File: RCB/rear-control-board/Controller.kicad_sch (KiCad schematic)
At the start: 27 parts, among them J6 Conn_01x05, U1 STM32F413CGUx, U2 LD1117S33TR_SOT223, U4 MCP2551-I-SN, Y1 Crystal

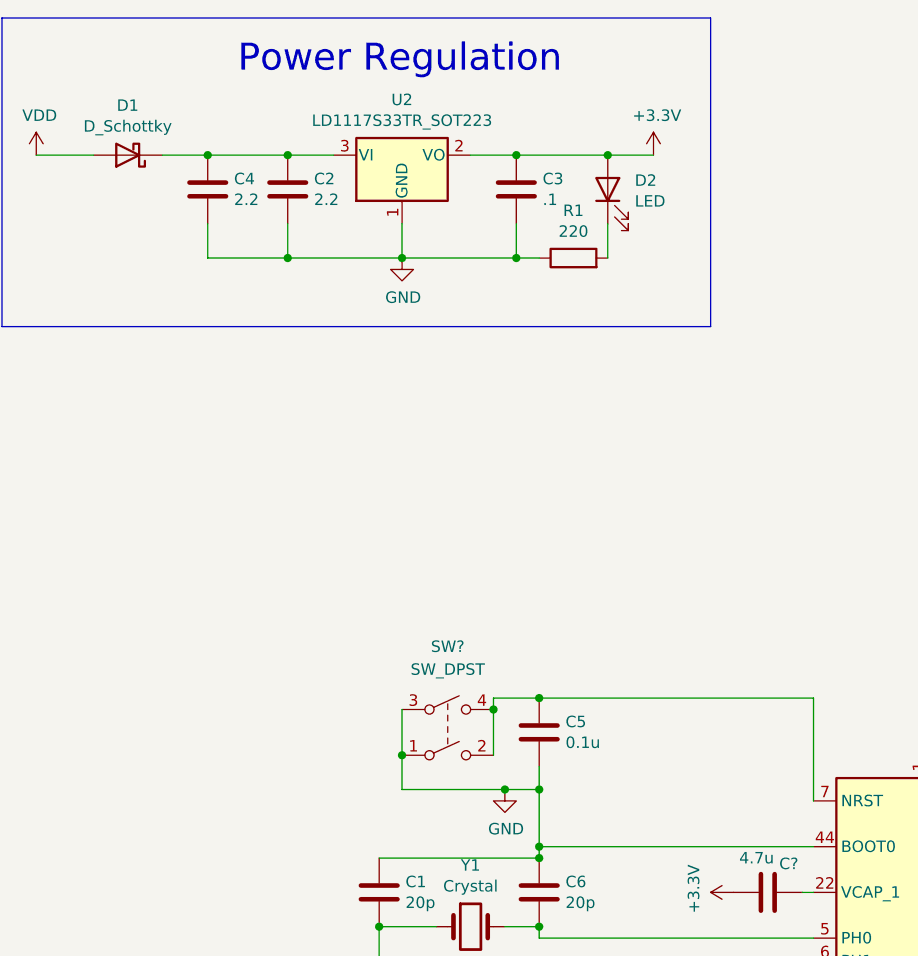
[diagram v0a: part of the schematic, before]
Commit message: power filtering and notes
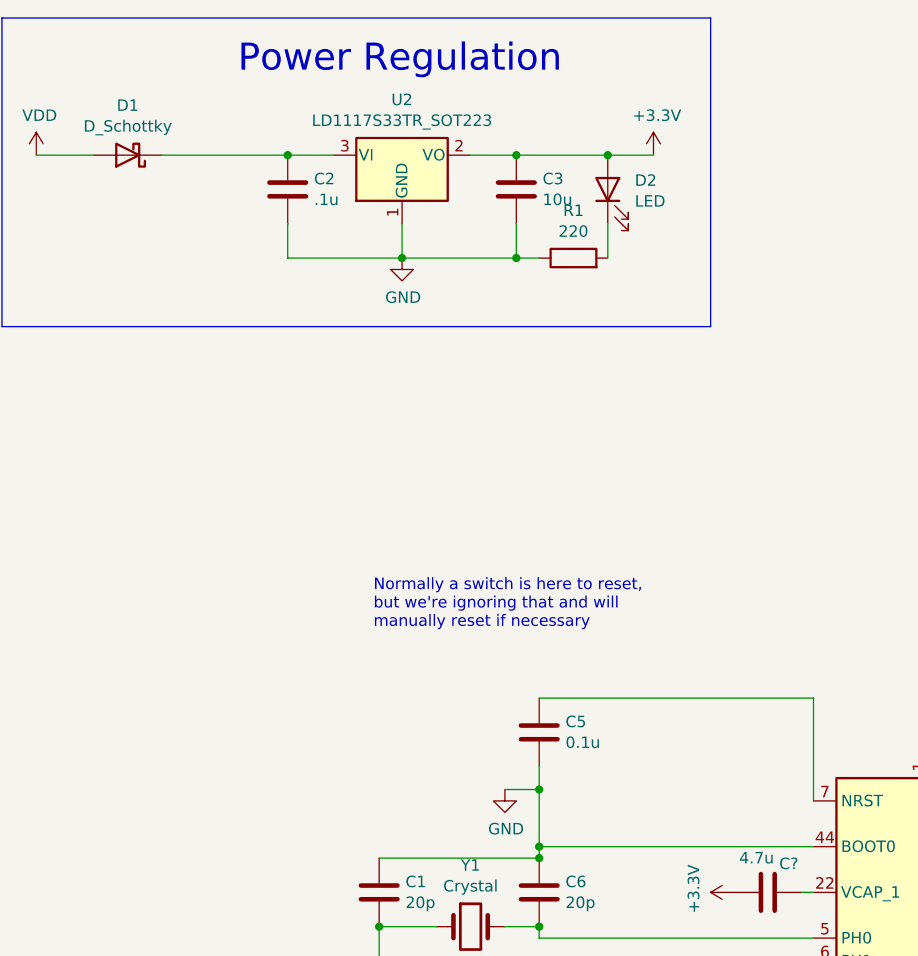
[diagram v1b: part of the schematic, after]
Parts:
- removed C4: 2.2, Capacitor_SMD:C_0603_1608Metric_Pad1.08x0.95mm_HandSolder, symbol Device:C
- removed SW?: SW_DPST, symbol Switch:SW_DPST
- C2: value 2.2 -> .1u
- C3: value .1 -> 10u
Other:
- note added: "Normally a switch is here to reset, but we're ignoring that and will manually reset if necessary"
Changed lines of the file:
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@@
   (junction (at 77.47 107.315) (diameter 0) (color 0 0 0 0)
   )
-  (junction (at 40.64 29.21) (diameter 0) (color 0 0 0 0)
-  )
   (junction (at 166.37 95.885) (diameter 0) (color 0 0 0 0)
   )
@@
   (junction (at 125.73 177.165) (diameter 0) (color 0 0 0 0)
   )
-  (junction (at 72.39 90.805) (diameter 0) (color 0 0 0 0)
-  )
-  (junction (at 77.47 89.535) (diameter 0) (color 0 0 0 0)
-  )
   (junction (at 269.24 152.4) (diameter 0) (color 0 0 0 0)
   )
-  (junction (at 73.66 99.695) (diameter 0) (color 0 0 0 0)
-  )
   (junction (at 74.93 29.21) (diameter 0) (color 0 0 0 0)
   )
@@
   (junction (at 123.19 177.165) (diameter 0) (color 0 0 0 0)
   )
-  (junction (at 62.23 95.885) (diameter 0) (color 0 0 0 0)
-  )
   (junction (at 269.24 128.27) (diameter 0) (color 0 0 0 0)
   )
@@
   (junction (at 77.47 99.695) (diameter 0) (color 0 0 0 0)
   )
-  (junction (at 49.53 40.64) (diameter 0) (color 0 0 0 0)
-  )
   (wire (pts (xy 234.95 153.67) (xy 251.46 153.67))
     (stroke (width 0) (type default) (color 0 0 0 0))
@@
     (stroke (width 0) (type default) (color 0 0 0 0))
   )
-  (wire (pts (xy 72.39 89.535) (xy 77.47 89.535))
-    (stroke (width 0) (type default) (color 0 0 0 0))
-  )
   (wire (pts (xy 274.955 125.73) (xy 275.59 125.73))
     (stroke (width 0) (type default) (color 0 0 0 0))
@@
     (stroke (width 0) (type default) (color 0 0 0 0))
   )
-  (wire (pts (xy 62.23 95.885) (xy 62.23 99.695))
-    (stroke (width 0) (type default) (color 0 0 0 0))
-  )
   (wire (pts (xy 144.78 141.605) (xy 140.97 141.605))
     (stroke (width 0) (type default) (color 0 0 0 0))
@@
     (stroke (width 0) (type default) (color 0 0 0 0))
   )
-  (wire (pts (xy 72.39 90.805) (xy 72.39 95.885))
-    (stroke (width 0) (type default) (color 0 0 0 0))
-  )
   (wire (pts (xy 166.37 81.915) (xy 171.45 81.915))
     (stroke (width 0) (type default) (color 0 0 0 0))
@@
     (stroke (width 0) (type default) (color 0 0 0 0))
   )
-  (wire (pts (xy 35.56 29.21) (xy 40.64 29.21))
-    (stroke (width 0) (type default) (color 0 0 0 0))
-  )
   (wire (pts (xy 120.65 177.165) (xy 120.65 174.625))
     (stroke (width 0) (type default) (color 0 0 0 0))
@@
     (stroke (width 0) (type default) (color 0 0 0 0))
   )
-  (wire (pts (xy 62.23 90.805) (xy 62.23 95.885))
-    (stroke (width 0) (type default) (color 0 0 0 0))
-  )
   (wire (pts (xy 140.97 136.525) (xy 144.78 136.525))
     (stroke (width 0) (type default) (color 0 0 0 0))
@@
     (stroke (width 0) (type default) (color 0 0 0 0))
   )
-  (wire (pts (xy 40.64 29.21) (xy 49.53 29.21))
+  (wire (pts (xy 35.56 29.21) (xy 49.53 29.21))
     (stroke (width 0) (type default) (color 0 0 0 0))
   )
@@
     (stroke (width 0) (type default) (color 0 0 0 0))
   )
-  (wire (pts (xy 40.64 40.64) (xy 49.53 40.64))
-    (stroke (width 0) (type default) (color 0 0 0 0))
-  )
   (wire (pts (xy 150.495 159.385) (xy 140.97 159.385))
     (stroke (width 0) (type default) (color 0 0 0 0))
@@
     (stroke (width 0) (type default) (color 0 0 0 0))
   )
-  (wire (pts (xy 62.23 99.695) (xy 73.66 99.695))
-    (stroke (width 0) (type default) (color 0 0 0 0))
-  )
   (polyline (pts (xy 278.13 161.29) (xy 278.13 109.22))
     (stroke (width 0) (type default) (color 0 0 0 0))
@@
     (stroke (width 0) (type default) (color 0 0 0 0))
   )
-  (wire (pts (xy 40.64 36.83) (xy 40.64 40.64))
-    (stroke (width 0) (type default) (color 0 0 0 0))
-  )
   (polyline (pts (xy 96.52 48.26) (xy 17.78 48.26))
     (stroke (width 0) (type default) (color 0 0 0 0))
@@
   )
   (wire (pts (xy 140.97 149.225) (xy 154.305 149.225))
-    (stroke (width 0) (type default) (color 0 0 0 0))
-  )
-  (wire (pts (xy 72.39 89.535) (xy 72.39 90.805))
     (stroke (width 0) (type default) (color 0 0 0 0))
   )
@@
   (text "CAN Transceiver" (at 242.57 114.3 0)
     (effects (font (size 2.0066 2.0066)) (justify left bottom))
+  )
+  (text "Normally a switch is here to reset,\nbut we're ignoring that and will \nmanually reset if necessary"
+    (at 59.055 81.915 0)
+    (effects (font (size 1.27 1.27)) (justify left bottom))
   )
   (text "IMD is low when clear, pull high\nBMS is high when clear, pull low"
@@
       (effects (font (size 1.27 1.27)) (justify left))
     )
-    (property "Value" "2.2" (id 1) (at 52.451 34.163 0)
+    (property "Value" ".1u" (id 1) (at 52.451 34.163 0)
       (effects (font (size 1.27 1.27)) (justify left))
     )
@@
       (effects (font (size 1.27 1.27)) (justify left))
     )
-    (property "Value" ".1" (id 1) (at 77.851 34.163 0)
+    (property "Value" "10u" (id 1) (at 77.851 34.163 0)
       (effects (font (size 1.27 1.27)) (justify left))
     )
@@
     (pin "2")
   )
-  (symbol (lib_id "Switch:SW_DPST") (at 67.31 93.345 0) (unit 1)
-    (in_bom yes) (on_board yes) (fields_autoplaced)
-    (property "Reference" "SW?" (id 0) (at 67.31 83.82 0))
-    (property "Value" "SW_DPST" (id 1) (at 67.31 86.36 0))
-    (property "Footprint" "" (id 2) (at 67.31 93.345 0)
-      (effects (font (size 1.27 1.27)) hide)
-    )
-    (property "Datasheet" "~" (id 3) (at 67.31 93.345 0)
-      (effects (font (size 1.27 1.27)) hide)
-    )
-    (pin "1")
-    (pin "2")
-    (pin "3")
-    (pin "4")
-  )
   (symbol (lib_id "power:+3.3V") (at 99.06 111.125 90) (unit 1)
     (in_bom yes) (on_board yes)
@@
     (pin "1")
   )
-  (symbol (lib_id "Device:C") (at 40.64 33.02 0) (unit 1)
-    (in_bom yes) (on_board yes)
-    (property "Reference" "C4" (id 0) (at 43.561 31.8516 0)
-      (effects (font (size 1.27 1.27)) (justify left))
-    )
-    (property "Value" "2.2" (id 1) (at 43.561 34.163 0)
-      (effects (font (size 1.27 1.27)) (justify left))
-    )
-    (property "Footprint" "Capacitor_SMD:C_0603_1608Metric_Pad1.08x0.95mm_HandSolder" (id 2) (at 41.6052 36.83 0)
-      (effects (font (size 1.27 1.27)) hide)
-    )
-    (property "Datasheet" "~" (id 3) (at 40.64 33.02 0)
-      (effects (font (size 1.27 1.27)) hide)
-    )
-    (pin "1")
-    (pin "2")
-  )
 )

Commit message: updating filtering cap layout
Kay suggested layout changes. Moved caps around
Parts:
- gave numbers to parts that had none: 1
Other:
- note added: "Power Caps Place as close as possible to the VDD pins"
- note removed: "Power Caps"
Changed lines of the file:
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@@
     (effects (font (size 2.9972 2.9972)) (justify left bottom))
   )
-  (text "Power Caps" (at 162.56 73.025 0)
+  (text "Power Caps\nPlace as close as possible to the VDD pins"
+    (at 154.305 73.66 0)
     (effects (font (size 1.27 1.27)) (justify left bottom))
   )
@@
   (symbol (lib_id "power:+3.3V") (at 99.06 111.125 90) (unit 1)
     (in_bom yes) (on_board yes)
-    (property "Reference" "#PWR?" (id 0) (at 102.87 111.125 0)
+    (property "Reference" "#PWR0142" (id 0) (at 102.87 111.125 0)
       (effects (font (size 1.27 1.27)) hide)
     )
@@
   (symbol (lib_id "Device:C") (at 102.87 111.125 270) (unit 1)
     (in_bom yes) (on_board yes)
-    (property "Reference" "C?" (id 0) (at 104.14 107.95 90)
-      (effects (font (size 1.27 1.27)) (justify left))
-    )
+    (property "Reference" "C4" (id 0) (at 104.14 107.95 90)
+      (effects (font (size 1.27 1.27)) (justify left))
+    )

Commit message: Major Review and Part Update
updating footprints, component values, layouts
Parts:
- removed C1, C6: 20p, Capacitor_SMD:C_0603_1608Metric_Pad1.08x0.95mm_HandSolder, symbol Device:C
- removed C8: 0.1u, Capacitor_SMD:C_0603_1608Metric_Pad1.08x0.95mm_HandSolder, symbol Device:C
- removed Y1: Crystal, Crystal:Crystal_HC49-U_Vertical, symbol Device:Crystal
- added Y1: CSTNE8M00, AERO_Footprints:Resonator_SMD_muRata_CSTxExxV-3Pin_3.0x1.1mm_HandSoldering, symbol Device:Resonator
- D1: value D_Schottky -> BAT54GW
- R1: value 220 -> 330
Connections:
- net GND: now also U1.8 (VSSA), Y1.2
- net at U1.5 (PH0): now also Y1.1
- net at U1.6 (PH1): now also Y1.3
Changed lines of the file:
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@@
 (kicad_sch (version 20211123) (generator eeschema)
   (paper "A4")
-  (junction (at 77.47 107.315) (diameter 0) (color 0 0 0 0)
+  (junction (at 128.27 177.165) (diameter 0) (color 0 0 0 0)
   )
   (junction (at 166.37 95.885) (diameter 0) (color 0 0 0 0)
@@
   (junction (at 80.01 136.525) (diameter 0) (color 0 0 0 0)
   )
-  (junction (at 140.97 84.455) (diameter 0) (color 0 0 0 0)
-  )
-  (junction (at 77.47 114.935) (diameter 0) (color 0 0 0 0)
-  )
   (junction (at 125.73 90.805) (diameter 0) (color 0 0 0 0)
   )
   (junction (at 80.01 133.985) (diameter 0) (color 0 0 0 0)
   )
-  (junction (at 59.69 114.935) (diameter 0) (color 0 0 0 0)
-  )
   (junction (at 49.53 29.21) (diameter 0) (color 0 0 0 0)
   )
@@
   (junction (at 166.37 81.915) (diameter 0) (color 0 0 0 0)
   )
-  (junction (at 143.51 92.075) (diameter 0) (color 0 0 0 0)
-  )
   (junction (at 77.47 106.045) (diameter 0) (color 0 0 0 0)
   )
@@
     (stroke (width 0) (type default) (color 0 0 0 0))
   )
-  (wire (pts (xy 140.97 84.455) (xy 146.05 84.455))
-    (stroke (width 0) (type default) (color 0 0 0 0))
-  )
   (wire (pts (xy 274.955 125.73) (xy 275.59 125.73))
     (stroke (width 0) (type default) (color 0 0 0 0))
@@
     (stroke (width 0) (type default) (color 0 0 0 0))
   )
-  (wire (pts (xy 77.47 114.935) (xy 73.66 114.935))
-    (stroke (width 0) (type default) (color 0 0 0 0))
-  )
   (wire (pts (xy 85.09 40.64) (xy 85.09 36.83))
     (stroke (width 0) (type default) (color 0 0 0 0))
@@
     (stroke (width 0) (type default) (color 0 0 0 0))
   )
-  (wire (pts (xy 59.69 114.935) (xy 66.04 114.935))
-    (stroke (width 0) (type default) (color 0 0 0 0))
-  )
-  (wire (pts (xy 143.51 92.075) (xy 146.05 92.075))
-    (stroke (width 0) (type default) (color 0 0 0 0))
-  )
   (wire (pts (xy 171.45 81.915) (xy 171.45 84.455))
     (stroke (width 0) (type default) (color 0 0 0 0))
@@
     (stroke (width 0) (type default) (color 0 0 0 0))
   )
-  (wire (pts (xy 59.69 118.745) (xy 107.95 118.745))
-    (stroke (width 0) (type default) (color 0 0 0 0))
-  )
   (wire (pts (xy 107.95 89.535) (xy 107.95 100.965))
     (stroke (width 0) (type default) (color 0 0 0 0))
@@
     (stroke (width 0) (type default) (color 0 0 0 0))
   )
+  (wire (pts (xy 73.66 107.315) (xy 77.47 107.315))
+    (stroke (width 0) (type default) (color 0 0 0 0))
+  )
   (polyline (pts (xy 128.905 18.415) (xy 128.905 54.61))
     (stroke (width 0) (type default) (color 0 0 0 0))
@@
     (stroke (width 0) (type default) (color 0 0 0 0))
   )
+  (wire (pts (xy 128.27 177.165) (xy 130.81 177.165))
+    (stroke (width 0) (type default) (color 0 0 0 0))
+  )
   (polyline (pts (xy 17.78 13.97) (xy 96.52 13.97))
     (stroke (width 0) (type default) (color 0 0 0 0))
@@
     (stroke (width 0) (type default) (color 0 0 0 0))
   )
+  (wire (pts (xy 73.66 109.855) (xy 73.66 107.315))
+    (stroke (width 0) (type default) (color 0 0 0 0))
+  )
   (wire (pts (xy 62.23 40.64) (xy 74.93 40.64))
     (stroke (width 0) (type default) (color 0 0 0 0))
@@
     (stroke (width 0) (type default) (color 0 0 0 0))
   )
+  (wire (pts (xy 69.85 114.935) (xy 69.85 118.745))
+    (stroke (width 0) (type default) (color 0 0 0 0))
+  )
   (wire (pts (xy 144.78 144.145) (xy 140.97 144.145))
     (stroke (width 0) (type default) (color 0 0 0 0))
@@
     (stroke (width 0) (type default) (color 0 0 0 0))
   )
+  (wire (pts (xy 130.81 177.165) (xy 130.81 174.625))
+    (stroke (width 0) (type default) (color 0 0 0 0))
+  )
   (wire (pts (xy 80.01 133.985) (xy 107.95 133.985))
     (stroke (width 0) (type default) (color 0 0 0 0))
@@
     (stroke (width 0) (type default) (color 0 0 0 0))
   )
-  (wire (pts (xy 59.69 114.935) (xy 59.69 118.745))
-    (stroke (width 0) (type default) (color 0 0 0 0))
-  )
   (wire (pts (xy 150.495 159.385) (xy 140.97 159.385))
     (stroke (width 0) (type default) (color 0 0 0 0))
@@
     (stroke (width 0) (type default) (color 0 0 0 0))
   )
+  (wire (pts (xy 69.85 118.745) (xy 107.95 118.745))
+    (stroke (width 0) (type default) (color 0 0 0 0))
+  )
   (polyline (pts (xy 278.13 161.29) (xy 278.13 109.22))
     (stroke (width 0) (type default) (color 0 0 0 0))
   )
   (wire (pts (xy 140.97 139.065) (xy 144.78 139.065))
-    (stroke (width 0) (type default) (color 0 0 0 0))
-  )
-  (wire (pts (xy 77.47 107.315) (xy 59.69 107.315))
     (stroke (width 0) (type default) (color 0 0 0 0))
   )
@@
     (in_bom yes) (on_board yes)
     (property "Reference" "D1" (id 0) (at 31.75 23.6982 0))
-    (property "Value" "D_Schottky" (id 1) (at 31.75 26.0096 0))
+    (property "Value" "BAT54GW" (id 1) (at 31.75 26.0096 0))
     (property "Footprint" "Diode_SMD:D_SMB" (id 2) (at 31.75 29.21 0)
       (effects (font (size 1.27 1.27)) hide)
@@
   (symbol (lib_id "Device:R") (at 81.28 40.64 90) (unit 1)
     (in_bom yes) (on_board yes)
-    (property "Reference" "R1" (id 0) (at 81.28 35.3822 90))
-    (property "Value" "220" (id 1) (at 81.28 37.6936 90))
+    (property "Reference" "R1" (id 0) (at 81.28 38.1 90))
+    (property "Value" "330" (id 1) (at 81.28 40.64 90))
     (property "Footprint" "Resistor_SMD:R_0603_1608Metric_Pad0.98x0.95mm_HandSolder" (id 2) (at 81.28 42.418 90)
       (effects (font (size 1.27 1.27)) hide)
@@
     )
     (pin "1")
-  )
-  (symbol (lib_id "Device:Crystal") (at 69.85 114.935 0) (unit 1)
-    (in_bom yes) (on_board yes)
-    (property "Reference" "Y1" (id 0) (at 69.85 108.1278 0))
-    (property "Value" "Crystal" (id 1) (at 69.85 110.4392 0))
-    (property "Footprint" "Crystal:Crystal_HC49-U_Vertical" (id 2) (at 69.85 114.935 0)
-      (effects (font (size 1.27 1.27)) hide)
-    )
-    (property "Datasheet" "~" (id 3) (at 69.85 114.935 0)
-      (effects (font (size 1.27 1.27)) hide)
-    )
-    (pin "1")
-    (pin "2")
-  )
-  (symbol (lib_id "Device:C") (at 59.69 111.125 0) (unit 1)
-    (in_bom yes) (on_board yes)
-    (property "Reference" "C1" (id 0) (at 62.611 109.9566 0)
-      (effects (font (size 1.27 1.27)) (justify left))
-    )
-    (property "Value" "20p" (id 1) (at 62.611 112.268 0)
-      (effects (font (size 1.27 1.27)) (justify left))
-    )
-    (property "Footprint" "Capacitor_SMD:C_0603_1608Metric_Pad1.08x0.95mm_HandSolder" (id 2) (at 60.6552 114.935 0)
-      (effects (font (size 1.27 1.27)) hide)
-    )
-    (property "Datasheet" "~" (id 3) (at 59.69 111.125 0)
-      (effects (font (size 1.27 1.27)) hide)
-    )
-    (pin "1")
-    (pin "2")
-  )
-  (symbol (lib_id "Device:C") (at 77.47 111.125 0) (unit 1)
-    (in_bom yes) (on_board yes)
-    (property "Reference" "C6" (id 0) (at 80.391 109.9566 0)
-      (effects (font (size 1.27 1.27)) (justify left))
-    )
-    (property "Value" "20p" (id 1) (at 80.391 112.268 0)
-      (effects (font (size 1.27 1.27)) (justify left))
-    )
-    (property "Footprint" "Capacitor_SMD:C_0603_1608Metric_Pad1.08x0.95mm_HandSolder" (id 2) (at 78.4352 114.935 0)
-      (effects (font (size 1.27 1.27)) hide)
-    )
-    (property "Datasheet" "~" (id 3) (at 77.47 111.125 0)
-      (effects (font (size 1.27 1.27)) hide)
-    )
-    (pin "1")
-    (pin "2")
   )
   (symbol (lib_id "power:+3.3V") (at 166.37 79.375 0) (unit 1)
@@
     (pin "1")
   )
-  (symbol (lib_id "Device:C") (at 146.05 88.265 180) (unit 1)
-    (in_bom yes) (on_board yes)
-    (property "Reference" "C8" (id 0) (at 151.13 89.535 0)
-      (effects (font (size 1.27 1.27)) (justify left))
-    )
-    (property "Value" "0.1u" (id 1) (at 152.4 86.995 0)
-      (effects (font (size 1.27 1.27)) (justify left))
-    )
-    (property "Footprint" "Capacitor_SMD:C_0603_1608Metric_Pad1.08x0.95mm_HandSolder" (id 2) (at 145.0848 84.455 0)
-      (effects (font (size 1.27 1.27)) hide)
-    )
-    (property "Datasheet" "~" (id 3) (at 146.05 88.265 0)
-      (effects (font (size 1.27 1.27)) hide)
-    )
-    (pin "1")
-    (pin "2")
-  )
   (symbol (lib_id "Device:C") (at 140.97 88.265 180) (unit 1)
     (in_bom yes) (on_board yes)
@@
     (pin "1")
   )
+  (symbol (lib_id "Device:Resonator") (at 73.66 114.935 180) (unit 1)
+    (in_bom yes) (on_board yes)
+    (property "Reference" "Y1" (id 0) (at 64.135 113.03 0))
+    (property "Value" "CSTNE8M00" (id 1) (at 64.77 109.22 0))
+    (property "Footprint" "AERO_Footprints:Resonator_SMD_muRata_CSTxExxV-3Pin_3.0x1.1mm_HandSoldering" (id 2) (at 74.295 114.935 0)
+      (effects (font (size 1.27 1.27)) hide)
+    )
+    (property "Datasheet" "~" (id 3) (at 74.295 114.935 0)
+      (effects (font (size 1.27 1.27)) hide)
+    )
+    (pin "1")
+    (pin "2")
+    (pin "3")
+  )
 )
